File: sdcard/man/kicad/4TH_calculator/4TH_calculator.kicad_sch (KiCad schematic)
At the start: 37 parts, among them SW0 SW_Push, SW1 SW_Push, SW10 SW_Push, SW11 SW_Push, SW12 SW_Push, SW13 SW_Push, SW14 SW_Push, SW15 SW_Push, SW16 SW_Push, SW17 SW_Push, SW19 SW_Push, SW2 SW_Push, SW20 SW_Push, SW21 SW_Push, SW22 SW_Push, SW23 SW_Push, SW24 SW_Push, SW25 SW_Push, SW26 SW_Push, SW27 SW_Push, SW28 SW_Push, SW29 SW_Push, SW3 SW_Push, SW30 SW_Push, SW31 SW_Push, SW32 SW_Push, SW33 SW_Push, SW34 SW_Push, SW4 SW_Push, SW5 SW_Push, SW6 SW_Push, SW7 SW_Push, SW8 SW_Push, SW9 SW_Push

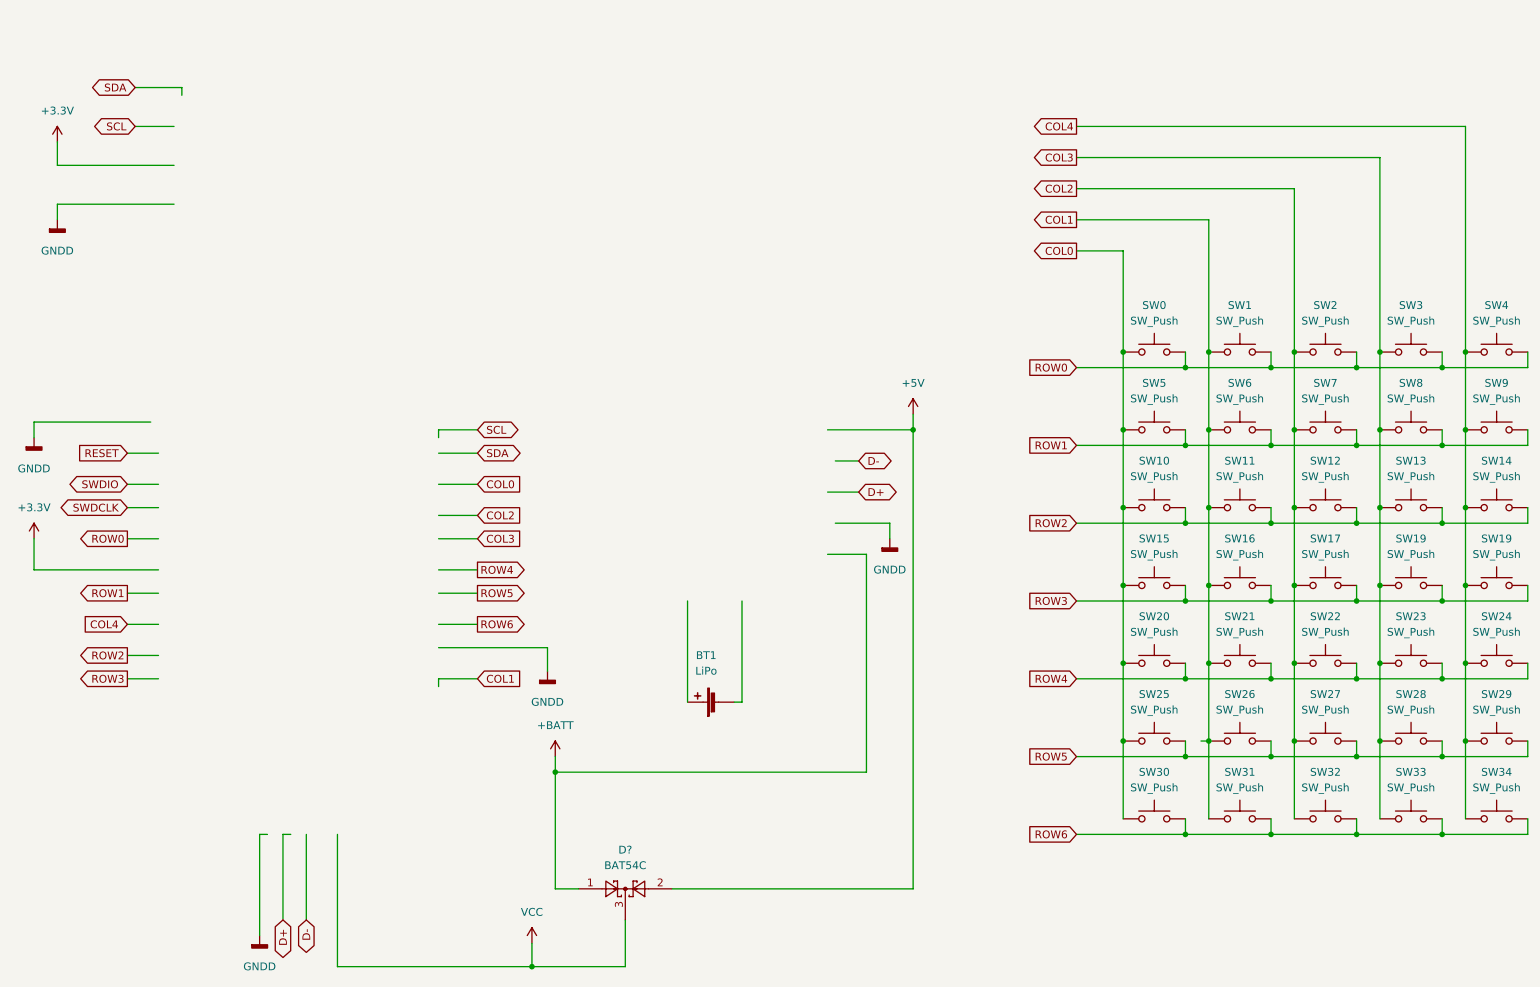
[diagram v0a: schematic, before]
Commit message: Use task critical for flash operations
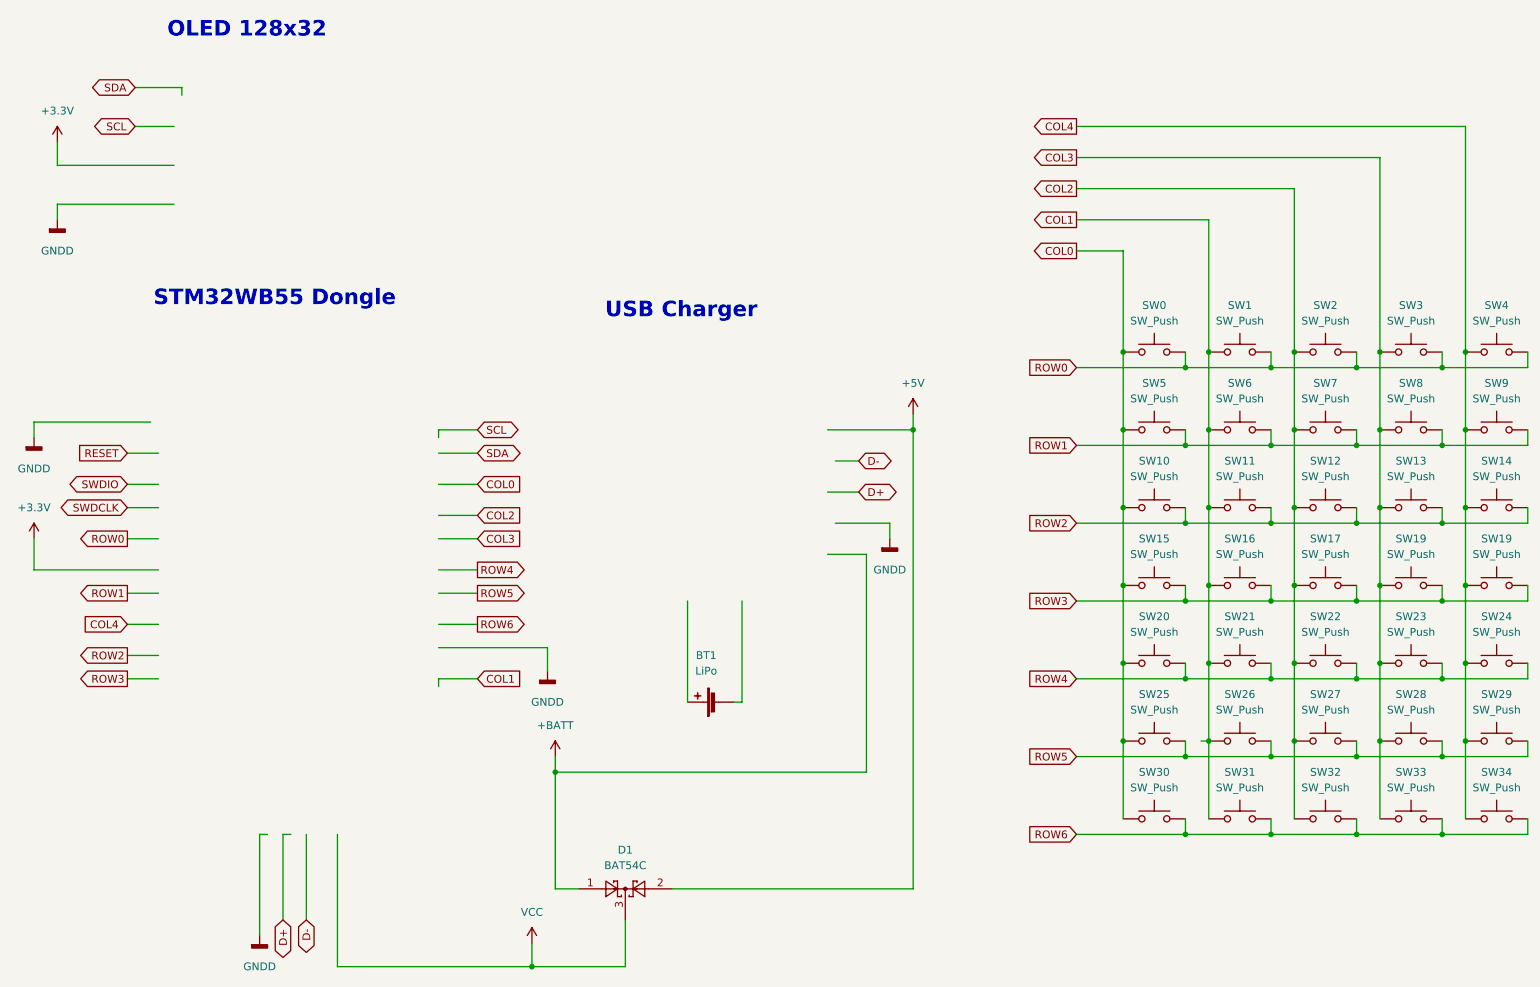
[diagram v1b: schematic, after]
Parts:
- gave numbers to parts that had none: 1
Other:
- note added: "OLED 128x32"
- note added: "STM32WB55 Dongle"
- note added: "USB Charger"
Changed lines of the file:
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@@
     )
+  )
+  (text "STM32WB55 Dongle" (at 38.5572 62.5856 0)
+    (effects (font (size 2.54 2.54) (thickness 0.508) bold) (justify left bottom))
+  )
+  (text "USB Charger" (at 112.268 64.5668 0)
+    (effects (font (size 2.54 2.54) (thickness 0.508) bold) (justify left bottom))
+  )
+  (text "OLED 128x32" (at 40.7924 18.7452 0)
+    (effects (font (size 2.54 2.54) (thickness 0.508) bold) (justify left bottom))
   )
   (global_label "ROW1" (shape input) (at 189.23 85.09 180) (fields_autoplaced)
@@
   (symbol (lib_id "Diode:BAT54C") (at 115.57 157.48 0) (unit 1)
     (in_bom yes) (on_board yes) (fields_autoplaced)
-    (property "Reference" "D?" (id 0) (at 115.57 151.13 0))
+    (property "Reference" "D1" (id 0) (at 115.57 151.13 0))
     (property "Value" "BAT54C" (id 1) (at 115.57 153.67 0))
     (property "Footprint" "Package_TO_SOT_SMD:SOT-23" (id 2) (at 117.475 154.305 0)
@@
     )
     (path "/7aa9121c-aed2-402f-b893-345eee594491"
-      (reference "D?") (unit 1) (value "BAT54C") (footprint "Package_TO_SOT_SMD:SOT-23")
+      (reference "D1") (unit 1) (value "BAT54C") (footprint "Package_TO_SOT_SMD:SOT-23")
     )
     (path "/660c362a-410c-4bd3-b29c-9c967e411400"
